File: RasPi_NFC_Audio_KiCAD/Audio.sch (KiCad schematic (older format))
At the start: 14 parts, among them J4 Screw_Terminal_01x02, J5 Screw_Terminal_01x02, U3 MAX98357, U4 MAX98357

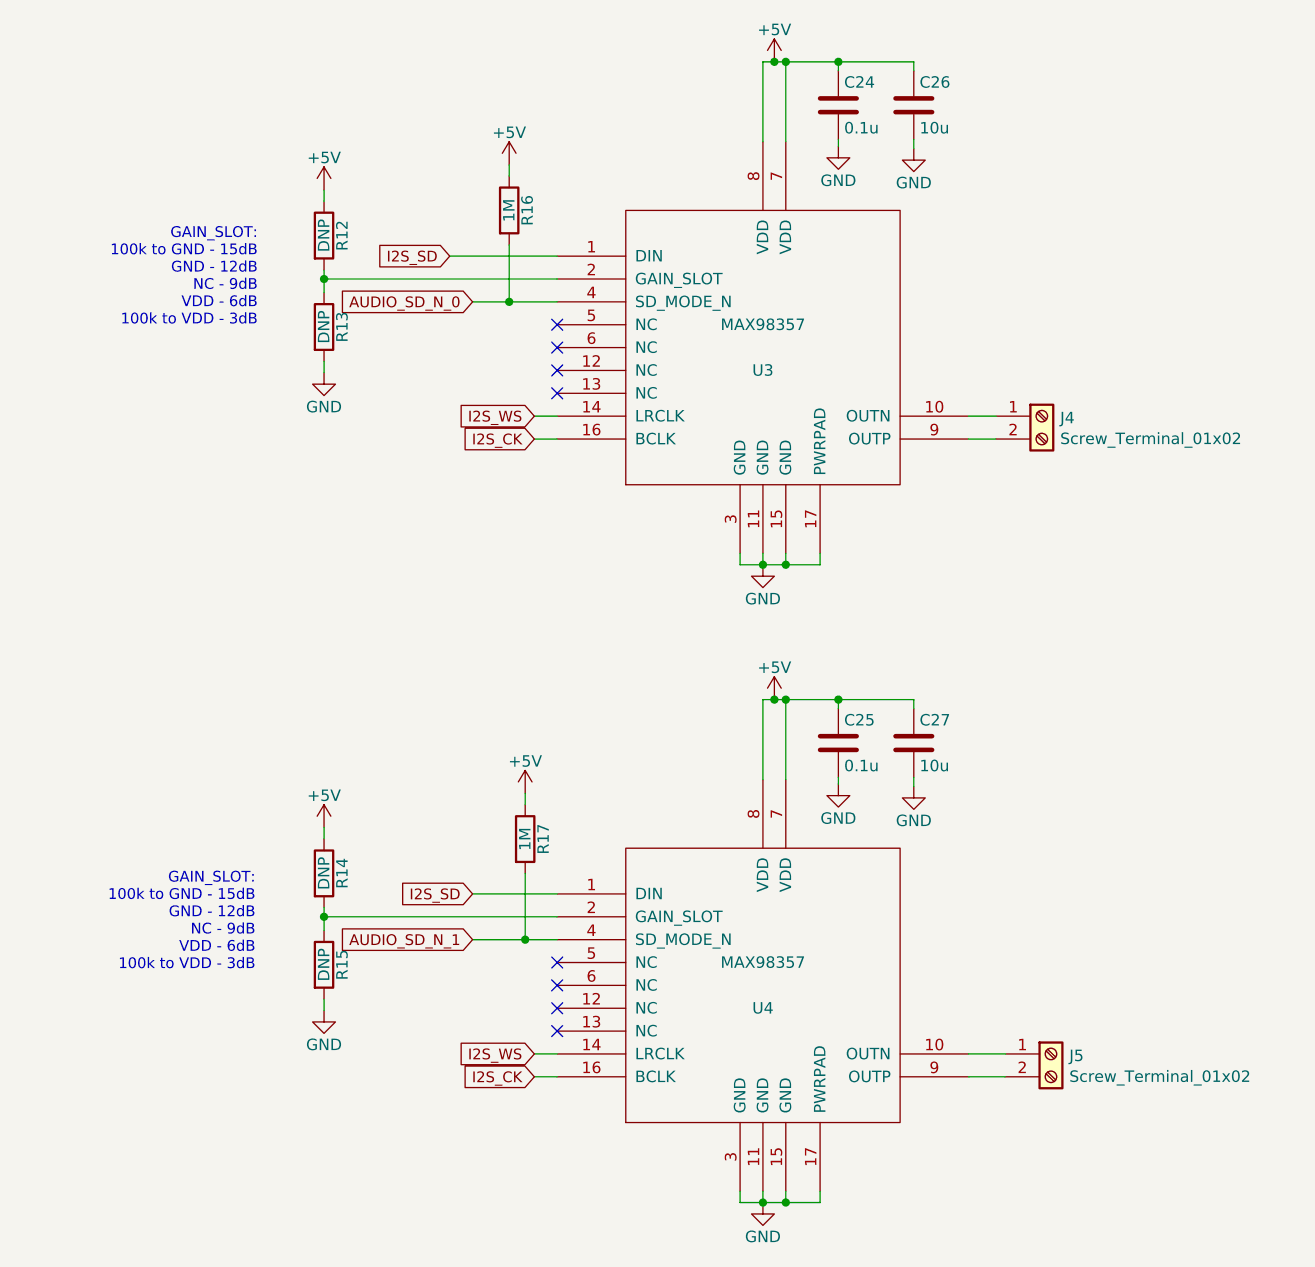
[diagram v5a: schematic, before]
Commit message: Schematic updates
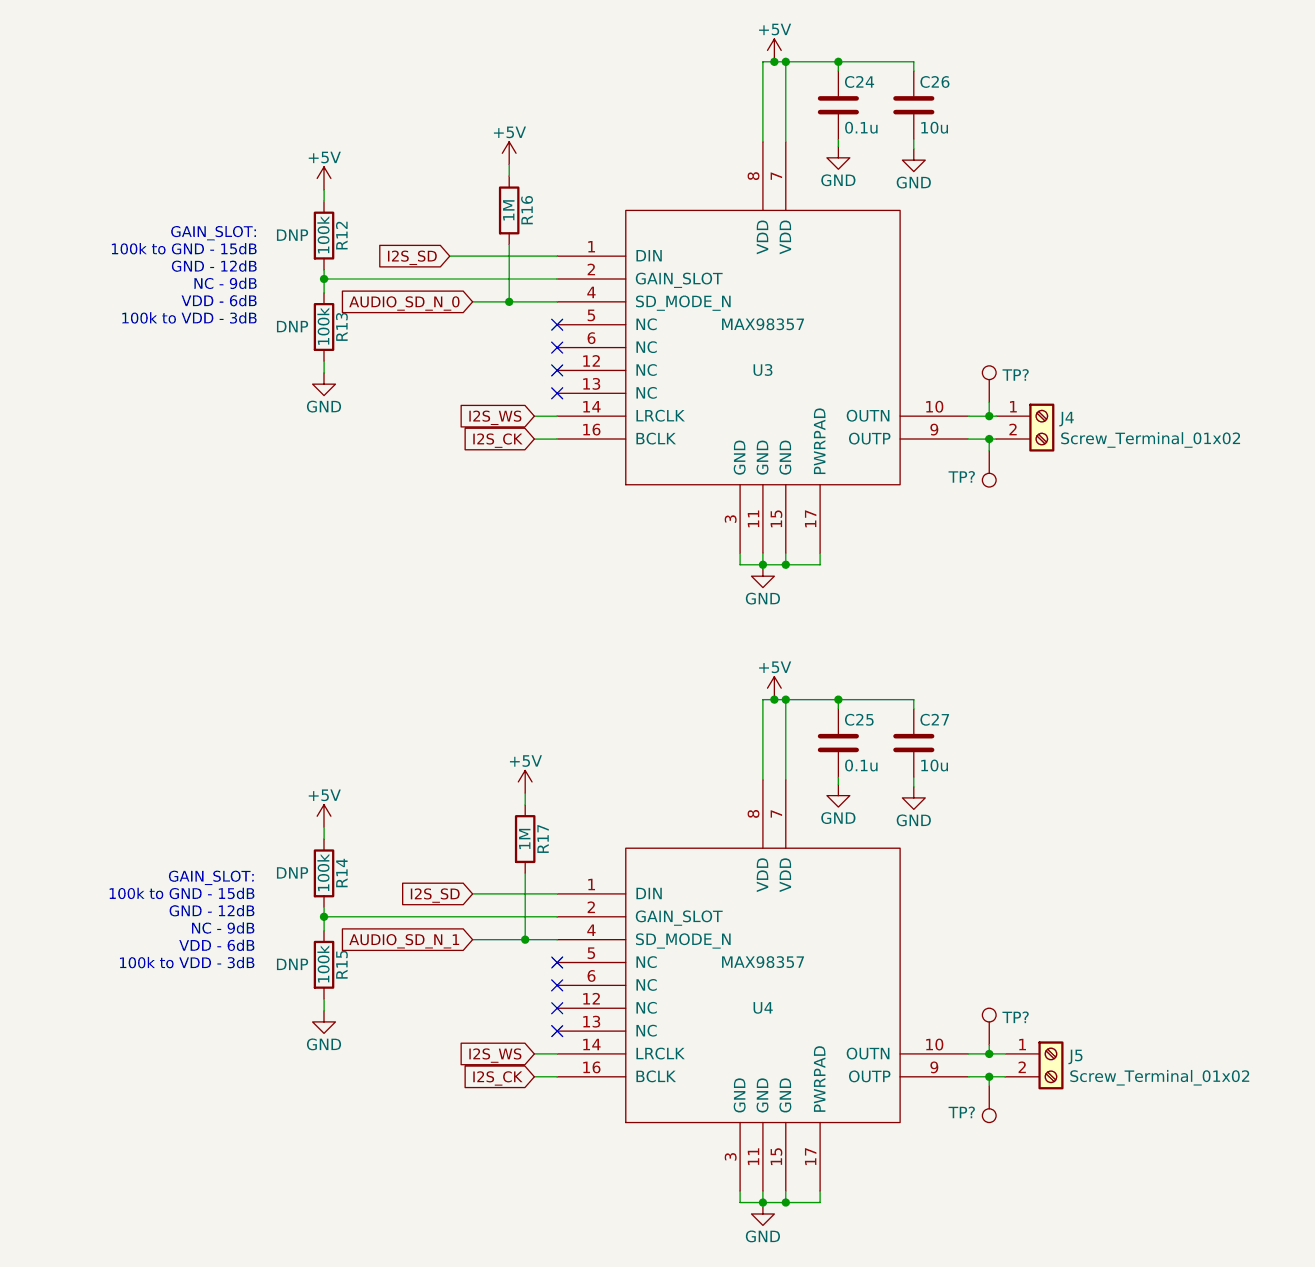
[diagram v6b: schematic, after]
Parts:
- added TP? (x4): TestPoint, symbol Connector:TestPoint
- J4, J5: DigiKey (none) -> A113320-ND; Part # (none) -> 282837-2
- R12, R13, R14, R15: value DNP -> 100k; DNP (none) -> DNP; DigiKey (none) -> RMCF0603FT100KCT-ND; Part # (none) -> RMCF0603FT100K
- R16, R17: DigiKey (none) -> 311-1.00MHRCT-ND; Part # (none) -> RC0603FR-071ML
- U3, U4: DigiKey (none) -> MAX98357AETE+TCT-ND; Part # (none) -> MAX98357AETE+T
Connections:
- net at J4.1 (Pin_1), U3.10 (OUTN): now also TP?.1
- net at J4.2 (Pin_2), U3.9 (OUTP): now also TP?.1
- net at J5.1 (Pin_1), U4.10 (OUTN): now also TP?.1
- net at J5.2 (Pin_2), U4.9 (OUTP): now also TP?.1
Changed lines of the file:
@@
 EESchema Schematic File Version 4
 LIBS:RasPi_NFC_Audio_KiCAD-cache
-EELAYER 30 0
+EELAYER 29 0
 EELAYER END
 $Descr A4 11693 8268
@@
 F 2 "CommandCenter:QFN50P300X300X80-17N" H 5490 2330 50  0001 C CNN
 F 3 "DOCUMENTATION" H 5490 2330 50  0001 C CNN
+F 4 "MAX98357AETE+T" H 5490 2330 50  0001 C CNN "Part #"
+F 5 "MAX98357AETE+TCT-ND" H 5490 2330 50  0001 C CNN "DigiKey"
 	1    5490 2330
 	1    0    0    -1
@@
 P 3570 1840
 F 0 "R12" V 3650 1840 50  0000 C CNN
-F 1 "DNP" V 3570 1840 50  0000 C CNN
+F 1 "100k" V 3570 1840 50  0000 C CNN
 F 2 "Resistor_SMD:R_0603_1608Metric_Pad1.05x0.95mm_HandSolder" V 3500 1840 50  0001 C CNN
 F 3 "" H 3570 1840 50  0001 C CNN
+F 4 "RMCF0603FT100K" H 3570 1840 50  0001 C CNN "Part #"
+F 5 "RMCF0603FT100KCT-ND" H 3570 1840 50  0001 C CNN "DigiKey"
+F 6 "DNP" H 3430 1840 50  0000 C CNN "DNP"
 	1    3570 1840
 	1    0    0    -1
@@
 P 3570 2240
 F 0 "R13" V 3650 2240 50  0000 C CNN
-F 1 "DNP" V 3570 2240 50  0000 C CNN
+F 1 "100k" V 3570 2240 50  0000 C CNN
 F 2 "Resistor_SMD:R_0603_1608Metric_Pad1.05x0.95mm_HandSolder" V 3500 2240 50  0001 C CNN
 F 3 "" H 3570 2240 50  0001 C CNN
+F 4 "RMCF0603FT100K" H 3570 2240 50  0001 C CNN "Part #"
+F 5 "RMCF0603FT100KCT-ND" H 3570 2240 50  0001 C CNN "DigiKey"
+F 6 "DNP" H 3430 2240 50  0000 C CNN "DNP"
 	1    3570 2240
 	1    0    0    -1
@@
 F 2 "CommandCenter:QFN50P300X300X80-17N" H 5490 5120 50  0001 C CNN
 F 3 "DOCUMENTATION" H 5490 5120 50  0001 C CNN
+F 4 "MAX98357AETE+T" H 5490 5120 50  0001 C CNN "Part #"
+F 5 "MAX98357AETE+TCT-ND" H 5490 5120 50  0001 C CNN "DigiKey"
 	1    5490 5120
 	1    0    0    -1
@@
 P 3570 4630
 F 0 "R14" V 3650 4630 50  0000 C CNN
-F 1 "DNP" V 3570 4630 50  0000 C CNN
+F 1 "100k" V 3570 4630 50  0000 C CNN
 F 2 "Resistor_SMD:R_0603_1608Metric_Pad1.05x0.95mm_HandSolder" V 3500 4630 50  0001 C CNN
 F 3 "" H 3570 4630 50  0001 C CNN
+F 4 "RMCF0603FT100K" H 3570 4630 50  0001 C CNN "Part #"
+F 5 "RMCF0603FT100KCT-ND" H 3570 4630 50  0001 C CNN "DigiKey"
+F 6 "DNP" H 3430 4630 50  0000 C CNN "DNP"
 	1    3570 4630
 	1    0    0    -1
@@
 P 3570 5030
 F 0 "R15" V 3650 5030 50  0000 C CNN
-F 1 "DNP" V 3570 5030 50  0000 C CNN
+F 1 "100k" V 3570 5030 50  0000 C CNN
 F 2 "Resistor_SMD:R_0603_1608Metric_Pad1.05x0.95mm_HandSolder" V 3500 5030 50  0001 C CNN
 F 3 "" H 3570 5030 50  0001 C CNN
+F 4 "RMCF0603FT100K" H 3570 5030 50  0001 C CNN "Part #"
+F 5 "RMCF0603FT100KCT-ND" H 3570 5030 50  0001 C CNN "DigiKey"
+F 6 "DNP" H 3430 5030 50  0000 C CNN "DNP"
 	1    3570 5030
 	1    0    0    -1
@@
 	3570 4820 3570 4880
 Wire Wire Line
-	6390 2630 6510 2630
-Wire Wire Line
-	6390 2730 6510 2730
-Wire Wire Line
-	6390 5420 6550 5420
-Wire Wire Line
-	6550 5520 6390 5520
+	6390 2630 6480 2630
+Wire Wire Line
+	6390 2730 6480 2730
+Wire Wire Line
+	6390 5420 6480 5420
+Wire Wire Line
+	6550 5520 6480 5520
 Wire Wire Line
 	3570 2030 4590 2030
@@
 F 2 "Resistor_SMD:R_0603_1608Metric_Pad1.05x0.95mm_HandSolder" V 4310 1730 50  0001 C CNN
 F 3 "" H 4380 1730 50  0001 C CNN
+F 4 "RC0603FR-071ML" H 4380 1730 50  0001 C CNN "Part #"
+F 5 "311-1.00MHRCT-ND" H 4380 1730 50  0001 C CNN "DigiKey"
 	1    4380 1730
 	1    0    0    -1
@@
 F 2 "Resistor_SMD:R_0603_1608Metric_Pad1.05x0.95mm_HandSolder" V 4380 4480 50  0001 C CNN
 F 3 "" H 4450 4480 50  0001 C CNN
+F 4 "RC0603FR-071ML" H 4450 4480 50  0001 C CNN "Part #"
+F 5 "311-1.00MHRCT-ND" H 4450 4480 50  0001 C CNN "DigiKey"
 	1    4450 4480
 	1    0    0    -1
@@
 F 2 "" H 6710 2630 50  0001 C CNN
 F 3 "~" H 6710 2630 50  0001 C CNN
+F 4 "282837-2" H 6710 2630 50  0001 C CNN "Part #"
+F 5 "A113320-ND" H 6710 2630 50  0001 C CNN "DigiKey"
 	1    6710 2630
 	1    0    0    -1
@@
 F 2 "" H 6750 5420 50  0001 C CNN
 F 3 "~" H 6750 5420 50  0001 C CNN
+F 4 "282837-2" H 6750 5420 50  0001 C CNN "Part #"
+F 5 "A113320-ND" H 6750 5420 50  0001 C CNN "DigiKey"
 	1    6750 5420
 	1    0    0    -1
 $EndComp
+$Comp
+L Connector:TestPoint TP?
+U 1 1 5E1D8095
+P 6480 2570
+AR Path="/5E17696B/5E1D8095" Ref="TP?"  Part="1"
+AR Path="/5E18E75B/5E1D8095" Ref="TP?"  Part="1"
+F 0 "TP?" H 6538 2688 50  0000 L CNN
+F 1 "TestPoint" H 6538 2597 50  0001 L CNN
+F 2 "" H 6680 2570 50  0001 C CNN
+F 3 "~" H 6680 2570 50  0001 C CNN
+	1    6480 2570
+	1    0    0    -1
+$EndComp
+Wire Wire Line
+	6480 2570 6480 2630
+Connection ~ 6480 2630
+Wire Wire Line
+	6480 2630 6510 2630
+$Comp
+L Connector:TestPoint TP?
+U 1 1 5E1DA818
+P 6480 2780
+AR Path="/5E17696B/5E1DA818" Ref="TP?"  Part="1"
+AR Path="/5E18E75B/5E1DA818" Ref="TP?"  Part="1"
+F 0 "TP?" H 6538 2898 50  0000 L CNN
+F 1 "TestPoint" H 6538 2807 50  0001 L CNN
+F 2 "" H 6680 2780 50  0001 C CNN
+F 3 "~" H 6680 2780 50  0001 C CNN
+	1    6480 2780
+	-1   0    0    1
+$EndComp
+Wire Wire Line
+	6480 2780 6480 2730
+Connection ~ 6480 2730
+Wire Wire Line
+	6480 2730 6510 2730
+$Comp
+L Connector:TestPoint TP?
+U 1 1 5E1DCFB9
+P 6480 5560
+AR Path="/5E17696B/5E1DCFB9" Ref="TP?"  Part="1"
+AR Path="/5E18E75B/5E1DCFB9" Ref="TP?"  Part="1"
+F 0 "TP?" H 6538 5678 50  0000 L CNN
+F 1 "TestPoint" H 6538 5587 50  0001 L CNN
+F 2 "" H 6680 5560 50  0001 C CNN
+F 3 "~" H 6680 5560 50  0001 C CNN
+	1    6480 5560
+	-1   0    0    1
+$EndComp
+$Comp
+L Connector:TestPoint TP?
+U 1 1 5E1DE537
+P 6480 5380
+AR Path="/5E17696B/5E1DE537" Ref="TP?"  Part="1"
+AR Path="/5E18E75B/5E1DE537" Ref="TP?"  Part="1"
+F 0 "TP?" H 6538 5498 50  0000 L CNN
+F 1 "TestPoint" H 6538 5407 50  0001 L CNN
+F 2 "" H 6680 5380 50  0001 C CNN
+F 3 "~" H 6680 5380 50  0001 C CNN
+	1    6480 5380
+	1    0    0    -1
+$EndComp
+Wire Wire Line
+	6480 5380 6480 5420
+Connection ~ 6480 5420
+Wire Wire Line
+	6480 5420 6550 5420
+Wire Wire Line
+	6480 5560 6480 5520
+Connection ~ 6480 5520
+Wire Wire Line
+	6480 5520 6390 5520
 $EndSCHEMATC

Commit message: Startednfootprint assignment
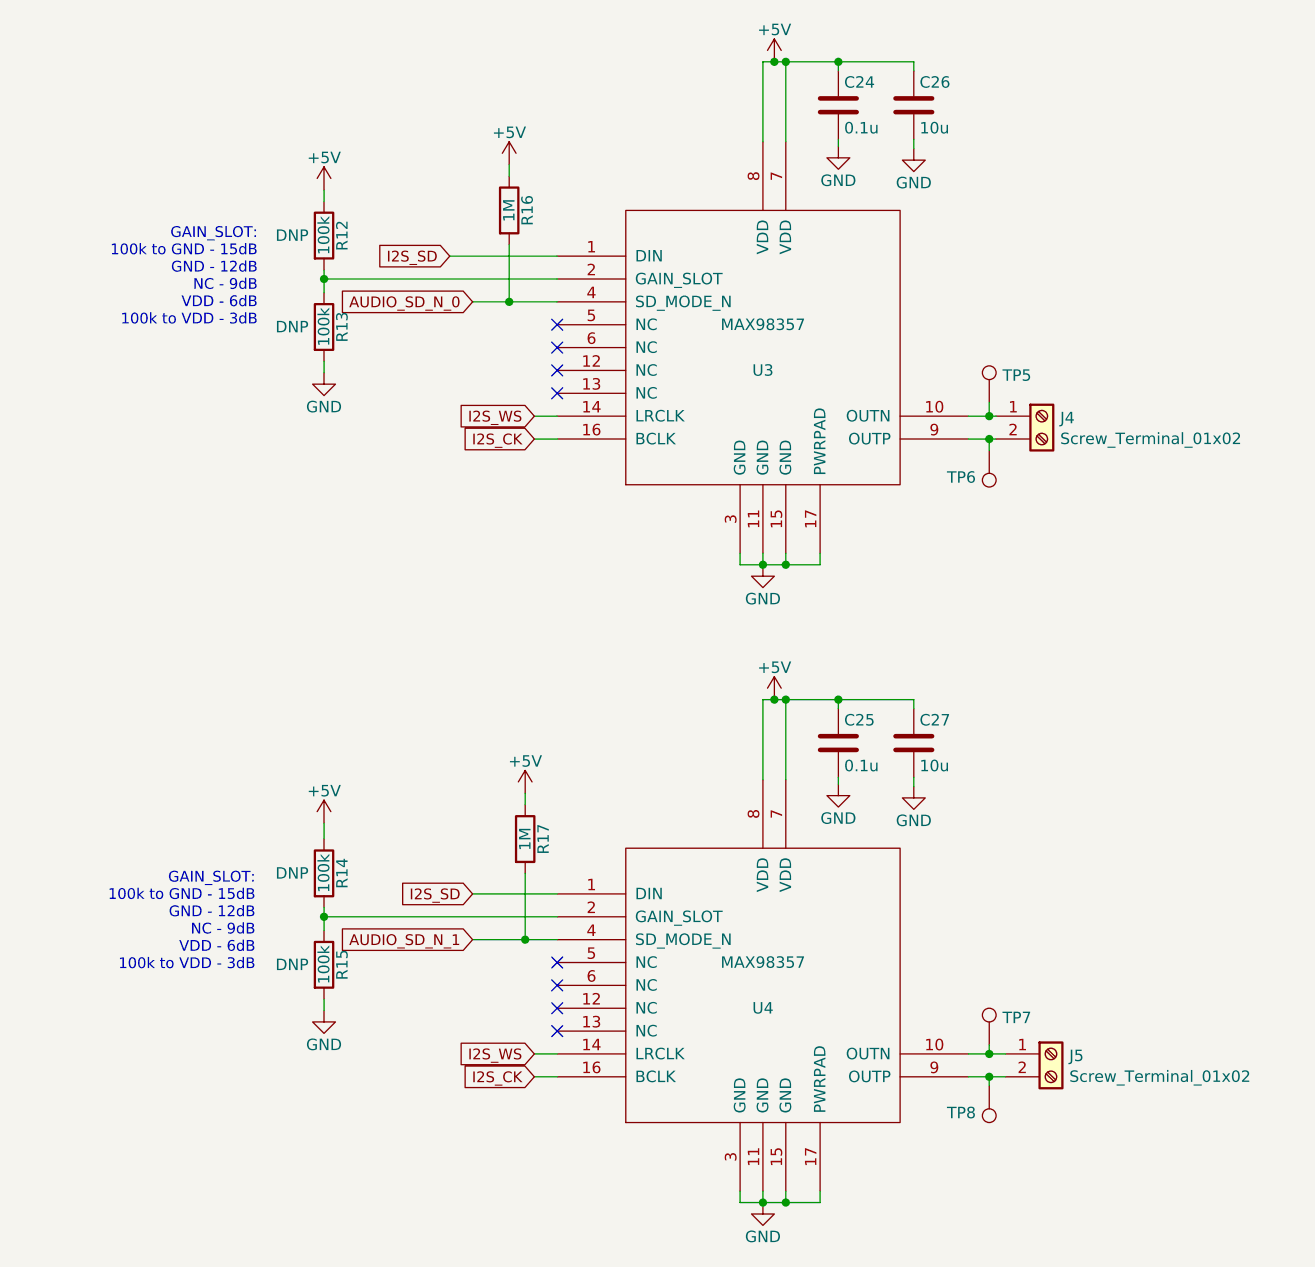
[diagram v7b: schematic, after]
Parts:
- U3, U4: footprint CommandCenter:QFN50P300X300X80-17N -> RasPi_NFC_Audio_PCB_Lib:QFN50P300X300X80-17N
- gave numbers to parts that had none: 4
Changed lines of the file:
@@
 F 0 "U3" H 5490 2230 50  0000 C CNN
 F 1 "MAX98357" H 5490 2430 50  0000 C CNN
-F 2 "CommandCenter:QFN50P300X300X80-17N" H 5490 2330 50  0001 C CNN
+F 2 "RasPi_NFC_Audio_PCB_Lib:QFN50P300X300X80-17N" H 5490 2330 50  0001 C CNN
 F 3 "DOCUMENTATION" H 5490 2330 50  0001 C CNN
 F 4 "MAX98357AETE+T" H 5490 2330 50  0001 C CNN "Part #"
@@
 F 0 "U4" H 5490 5020 50  0000 C CNN
 F 1 "MAX98357" H 5490 5220 50  0000 C CNN
-F 2 "CommandCenter:QFN50P300X300X80-17N" H 5490 5120 50  0001 C CNN
+F 2 "RasPi_NFC_Audio_PCB_Lib:QFN50P300X300X80-17N" H 5490 5120 50  0001 C CNN
 F 3 "DOCUMENTATION" H 5490 5120 50  0001 C CNN
 F 4 "MAX98357AETE+T" H 5490 5120 50  0001 C CNN "Part #"
@@
 L power:+5V #PWR0143
 U 1 1 5CC7543D
-P 3570 4430
-F 0 "#PWR0143" H 3570 4280 50  0001 C CNN
-F 1 "+5V" H 3570 4570 50  0000 C CNN
-F 2 "" H 3570 4430 50  0001 C CNN
-F 3 "" H 3570 4430 50  0001 C CNN
-	1    3570 4430
-	1    0    0    -1
-$EndComp
-Wire Wire Line
-	3570 4480 3570 4430
+P 3570 4410
+F 0 "#PWR0143" H 3570 4260 50  0001 C CNN
+F 1 "+5V" H 3570 4550 50  0000 C CNN
+F 2 "" H 3570 4410 50  0001 C CNN
+F 3 "" H 3570 4410 50  0001 C CNN
+	1    3570 4410
+	1    0    0    -1
+$EndComp
+Wire Wire Line
+	3570 4480 3570 4410
 Wire Wire Line
 	3570 5180 3570 5230
@@
 P 6480 2570
 AR Path="/5E17696B/5E1D8095" Ref="TP?"  Part="1"
-AR Path="/5E18E75B/5E1D8095" Ref="TP?"  Part="1"
-F 0 "TP?" H 6538 2688 50  0000 L CNN
+AR Path="/5E18E75B/5E1D8095" Ref="TP5"  Part="1"
+F 0 "TP5" H 6538 2688 50  0000 L CNN
 F 1 "TestPoint" H 6538 2597 50  0001 L CNN
 F 2 "" H 6680 2570 50  0001 C CNN
@@
 P 6480 2780
 AR Path="/5E17696B/5E1DA818" Ref="TP?"  Part="1"
-AR Path="/5E18E75B/5E1DA818" Ref="TP?"  Part="1"
-F 0 "TP?" H 6538 2898 50  0000 L CNN
+AR Path="/5E18E75B/5E1DA818" Ref="TP6"  Part="1"
+F 0 "TP6" H 6538 2898 50  0000 L CNN
 F 1 "TestPoint" H 6538 2807 50  0001 L CNN
 F 2 "" H 6680 2780 50  0001 C CNN
@@
 P 6480 5560
 AR Path="/5E17696B/5E1DCFB9" Ref="TP?"  Part="1"
-AR Path="/5E18E75B/5E1DCFB9" Ref="TP?"  Part="1"
-F 0 "TP?" H 6538 5678 50  0000 L CNN
+AR Path="/5E18E75B/5E1DCFB9" Ref="TP8"  Part="1"
+F 0 "TP8" H 6538 5678 50  0000 L CNN
 F 1 "TestPoint" H 6538 5587 50  0001 L CNN
 F 2 "" H 6680 5560 50  0001 C CNN
@@
 P 6480 5380
 AR Path="/5E17696B/5E1DE537" Ref="TP?"  Part="1"
-AR Path="/5E18E75B/5E1DE537" Ref="TP?"  Part="1"
-F 0 "TP?" H 6538 5498 50  0000 L CNN
+AR Path="/5E18E75B/5E1DE537" Ref="TP7"  Part="1"
+F 0 "TP7" H 6538 5498 50  0000 L CNN
 F 1 "TestPoint" H 6538 5407 50  0001 L CNN
 F 2 "" H 6680 5380 50  0001 C CNN

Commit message: Layout started
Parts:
- J4, J5: footprint (none) -> TerminalBlock_TE-Connectivity:TerminalBlock_TE_282834-2_1x02_P2.54mm_Horizontal; DigiKey A113320-ND -> A98333-ND; Part # 282837-2 -> 282834-2
- TP5, TP6, TP7, TP8: footprint (none) -> TestPoint:TestPoint_Keystone_5019_Minature
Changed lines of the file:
@@
 F 0 "J4" H 6790 2622 50  0000 L CNN
 F 1 "Screw_Terminal_01x02" H 6790 2531 50  0000 L CNN
-F 2 "" H 6710 2630 50  0001 C CNN
+F 2 "TerminalBlock_TE-Connectivity:TerminalBlock_TE_282834-2_1x02_P2.54mm_Horizontal" H 6710 2630 50  0001 C CNN
 F 3 "~" H 6710 2630 50  0001 C CNN
-F 4 "282837-2" H 6710 2630 50  0001 C CNN "Part #"
-F 5 "A113320-ND" H 6710 2630 50  0001 C CNN "DigiKey"
+F 4 "282834-2" H 6710 2630 50  0001 C CNN "Part #"
+F 5 "A98333-ND" H 6710 2630 50  0001 C CNN "DigiKey"
 	1    6710 2630
 	1    0    0    -1
@@
 F 0 "J5" H 6830 5412 50  0000 L CNN
 F 1 "Screw_Terminal_01x02" H 6830 5321 50  0000 L CNN
-F 2 "" H 6750 5420 50  0001 C CNN
+F 2 "TerminalBlock_TE-Connectivity:TerminalBlock_TE_282834-2_1x02_P2.54mm_Horizontal" H 6750 5420 50  0001 C CNN
 F 3 "~" H 6750 5420 50  0001 C CNN
-F 4 "282837-2" H 6750 5420 50  0001 C CNN "Part #"
-F 5 "A113320-ND" H 6750 5420 50  0001 C CNN "DigiKey"
+F 4 "282834-2" H 6750 5420 50  0001 C CNN "Part #"
+F 5 "A98333-ND" H 6750 5420 50  0001 C CNN "DigiKey"
 	1    6750 5420
 	1    0    0    -1
@@
 F 0 "TP5" H 6538 2688 50  0000 L CNN
 F 1 "TestPoint" H 6538 2597 50  0001 L CNN
-F 2 "" H 6680 2570 50  0001 C CNN
+F 2 "TestPoint:TestPoint_Keystone_5019_Minature" H 6680 2570 50  0001 C CNN
 F 3 "~" H 6680 2570 50  0001 C CNN
 	1    6480 2570
@@
 F 0 "TP6" H 6538 2898 50  0000 L CNN
 F 1 "TestPoint" H 6538 2807 50  0001 L CNN
-F 2 "" H 6680 2780 50  0001 C CNN
+F 2 "TestPoint:TestPoint_Keystone_5019_Minature" H 6680 2780 50  0001 C CNN
 F 3 "~" H 6680 2780 50  0001 C CNN
 	1    6480 2780
@@
 F 0 "TP8" H 6538 5678 50  0000 L CNN
 F 1 "TestPoint" H 6538 5587 50  0001 L CNN
-F 2 "" H 6680 5560 50  0001 C CNN
+F 2 "TestPoint:TestPoint_Keystone_5019_Minature" H 6680 5560 50  0001 C CNN
 F 3 "~" H 6680 5560 50  0001 C CNN
 	1    6480 5560
@@
 F 0 "TP7" H 6538 5498 50  0000 L CNN
 F 1 "TestPoint" H 6538 5407 50  0001 L CNN
-F 2 "" H 6680 5380 50  0001 C CNN
+F 2 "TestPoint:TestPoint_Keystone_5019_Minature" H 6680 5380 50  0001 C CNN
 F 3 "~" H 6680 5380 50  0001 C CNN
 	1    6480 5380
